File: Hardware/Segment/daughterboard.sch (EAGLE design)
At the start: 1 part, among them IC1 PBQ79656PAPTQ1

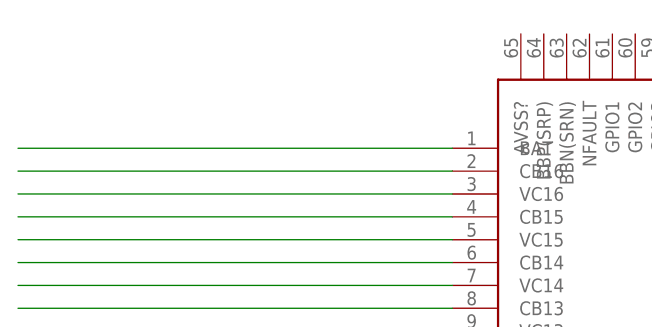
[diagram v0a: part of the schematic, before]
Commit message: added a resistor
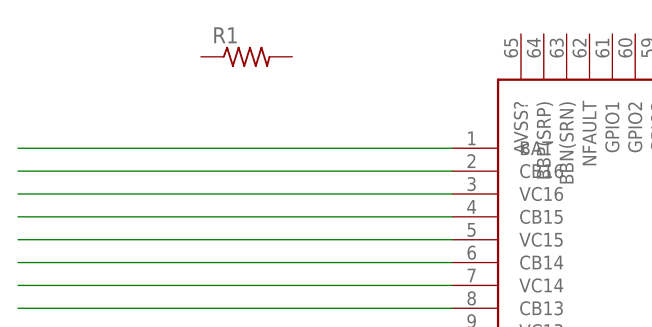
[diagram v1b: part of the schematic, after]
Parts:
- added R1: (no value), rcl:R-US_R0603
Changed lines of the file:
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@@
 <layers>
 <layer number="1" name="Top" color="4" fill="1" visible="no" active="no"/>
+<layer number="2" name="Route2" color="1" fill="3" visible="no" active="no"/>
+<layer number="3" name="Route3" color="4" fill="3" visible="no" active="no"/>
+<layer number="4" name="Route4" color="1" fill="4" visible="no" active="no"/>
+<layer number="5" name="Route5" color="4" fill="4" visible="no" active="no"/>
+<layer number="6" name="Route6" color="1" fill="8" visible="no" active="no"/>
+<layer number="7" name="Route7" color="4" fill="8" visible="no" active="no"/>
+<layer number="8" name="Route8" color="1" fill="2" visible="no" active="no"/>
+<layer number="9" name="Route9" color="4" fill="2" visible="no" active="no"/>
+<layer number="10" name="Route10" color="1" fill="7" visible="no" active="no"/>
+<layer number="11" name="Route11" color="4" fill="7" visible="no" active="no"/>
+<layer number="12" name="Route12" color="1" fill="5" visible="no" active="no"/>
+<layer number="13" name="Route13" color="4" fill="5" visible="no" active="no"/>
+<layer number="14" name="Route14" color="1" fill="6" visible="no" active="no"/>
+<layer number="15" name="Route15" color="4" fill="6" visible="no" active="no"/>
 <layer number="16" name="Bottom" color="1" fill="1" visible="no" active="no"/>
 <layer number="17" name="Pads" color="2" fill="1" visible="no" active="no"/>
@@
 <parts>
 <part name="IC1" library="PBQ79656PAPTQ1" deviceset="PBQ79656PAPTQ1" device=""/>
+<part name="R1" library="rcl" library_urn="urn:adsk.eagle:library:334" deviceset="R-US_" device="R0603" package3d_urn="urn:adsk.eagle:package:23555/3"/>
 </parts>
 <sheets>
@@
 <attribute name="VALUE" x="107.95" y="83.82" size="1.778" layer="96" align="center-left"/>
 </instance>
+<instance part="R1" gate="G$1" x="33.02" y="83.82" smashed="yes">
+<attribute name="NAME" x="29.21" y="85.3186" size="1.778" layer="95"/>
+<attribute name="VALUE" x="29.21" y="80.518" size="1.778" layer="96"/>
+</instance>
 </instances>
 <busses>
@@
 </schematic>
 </drawing>
+<compatibility>
+<note version="8.2" severity="warning">
+Since Version 8.2, EAGLE supports online libraries. The ids
+of those online libraries will not be understood (or retained)
+with this version.
+</note>
+<note version="8.3" severity="warning">
+Since Version 8.3, EAGLE supports URNs for individual library
+assets (packages, symbols, and devices). The URNs of those assets
+will not be understood (or retained) with this version.
+</note>
+<note version="8.3" severity="warning">
+Since Version 8.3, EAGLE supports the association of 3D packages
+with devices in libraries, schematics, and board files. Those 3D
+packages will not be understood (or retained) with this version.
+</note>
+<note version="8.4" severity="warning">
+Since Version 8.4, EAGLE supports properties for SPICE simulation.
+Probes in schematics and SPICE mapping objects found in parts and library devices
+will not be understood with this version. Update EAGLE to the latest version
+for full support of SPICE simulation.
+</note>
+</compatibility>
 </eagle>

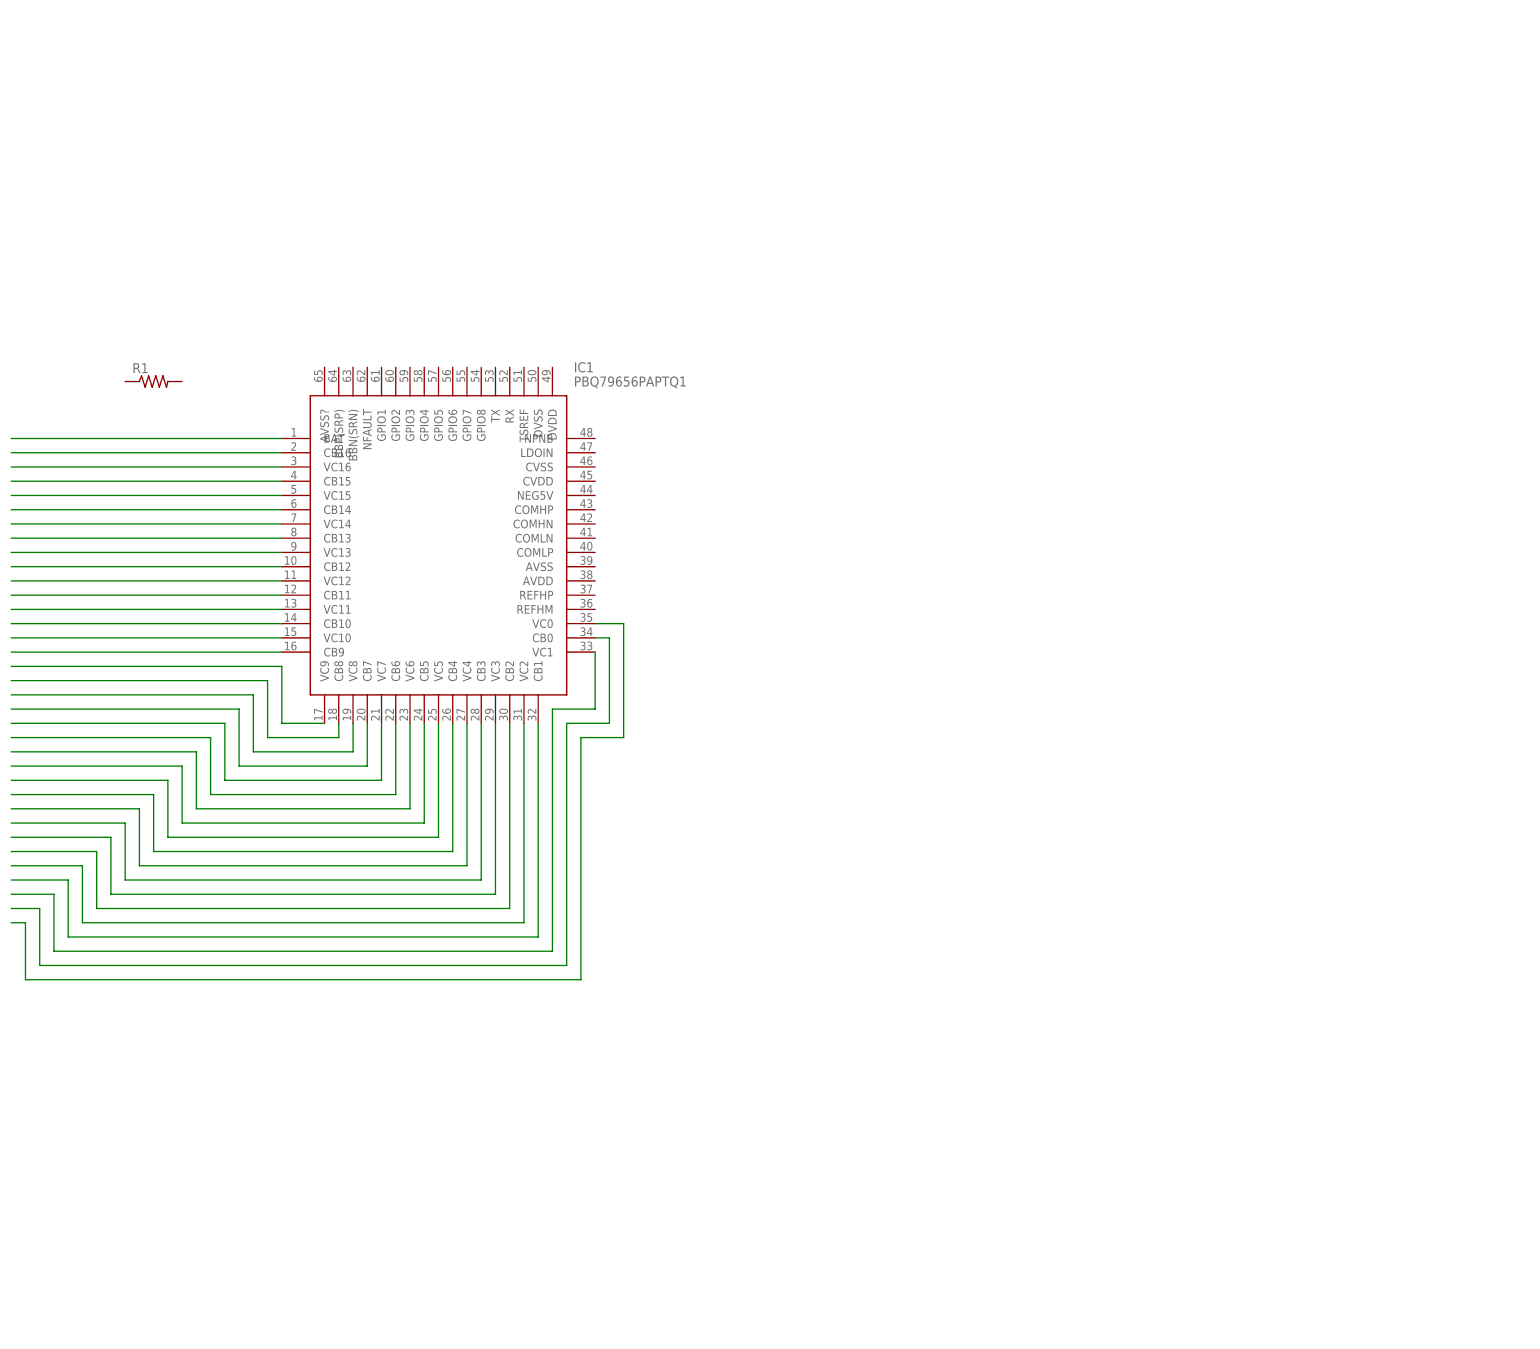
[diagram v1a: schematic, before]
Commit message: Connected IC to 10 battery cells
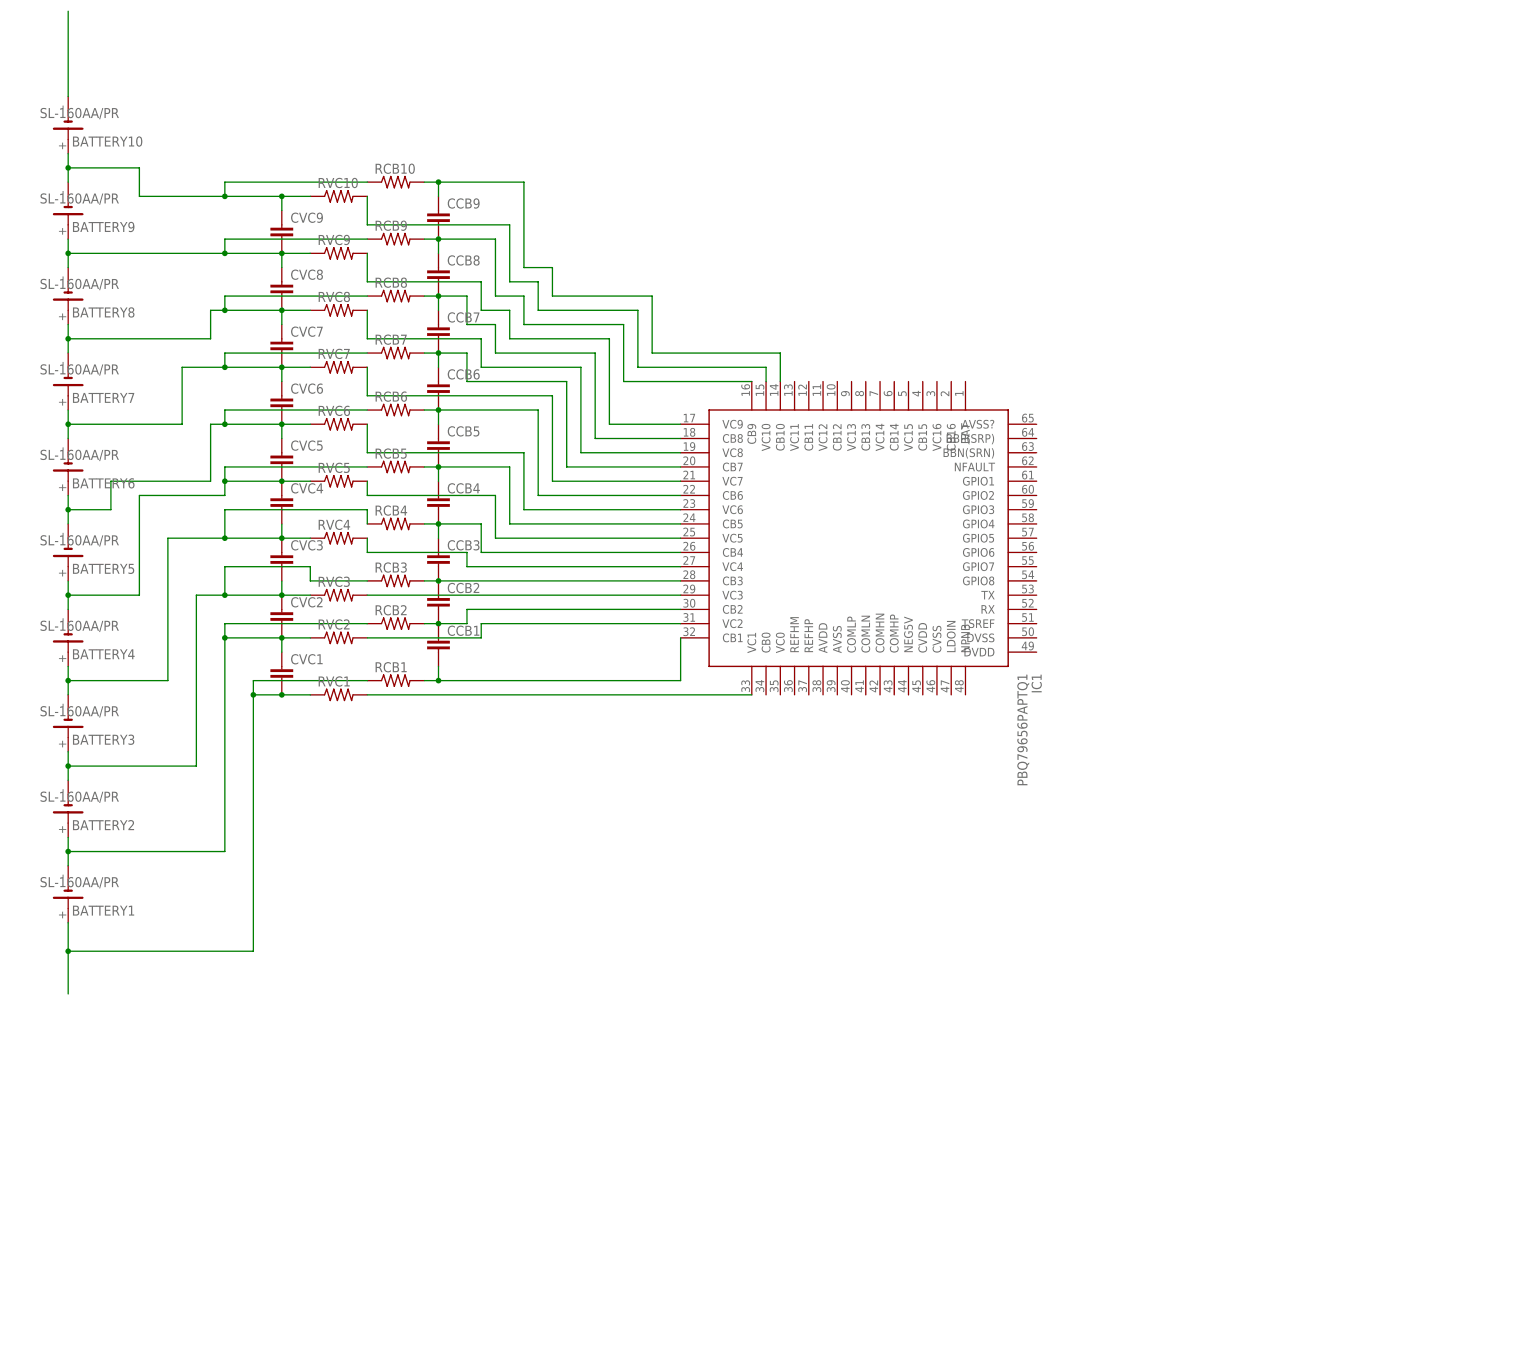
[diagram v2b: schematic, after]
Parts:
- removed R1: (no value), rcl:R-US_R0603
- added BATTERY1, BATTERY10, BATTERY2, BATTERY3, BATTERY4, BATTERY5, BATTERY6, BATTERY7, BATTERY8, BATTERY9: SL-160AA/PR, battery:SL-160AA/PR
- added CCB1, CCB2, CCB3, CCB4, CCB5, CCB6, CCB7, CCB8, CCB9, CVC1, CVC2, CVC3, CVC4, CVC5, CVC6, CVC7, CVC8, CVC9: (no value), capacitor-wima:C2.5/2
- added RCB1, RCB10, RCB2, RCB3, RCB4, RCB5, RCB6, RCB7, RCB8, RCB9, RVC1, RVC10, RVC2, RVC3, RVC4, RVC5, RVC6, RVC7, RVC8, RVC9: (no value), rcl:R-US_R0603
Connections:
- removed net N$25: IC1.VC5
- removed net N$33: IC1.VC1
- removed net N$34: IC1.CB0
- removed net N$35: IC1.VC0
- net N$1: now also IC1.VC1, RVC1.2; no longer IC1.BAT
- net N$10: now also IC1.VC4, RVC4.2; no longer IC1.CB12
- net N$11: now also CCB6.1, CCB7.2, IC1.CB7, RCB7.2; no longer IC1.VC12
- net N$12: now also BATTERY3.-, BATTERY4.+, CVC3.1, CVC4.2, RCB4.1, RVC4.1; no longer IC1.CB11
- net N$13: now also CCB3.1, CCB4.2, IC1.CB4, RCB4.2; no longer IC1.VC11
- net N$14: now also IC1.VC5, RVC5.2; no longer IC1.CB10
- net N$15: now also BATTERY4.-, BATTERY5.+, CVC4.1, CVC5.2, RCB5.1, RVC5.1; no longer IC1.VC10
- net N$16: now also CCB4.1, CCB5.2, IC1.CB5, RCB5.2; no longer IC1.CB9
- net N$17: now also IC1.VC8, RVC8.2; no longer IC1.VC9
- net N$18: now also BATTERY7.-, BATTERY8.+, CVC7.1, CVC8.2, RCB8.1, RVC8.1; no longer IC1.CB8
- net N$19: now also CCB7.1, CCB8.2, IC1.CB8, RCB8.2; no longer IC1.VC8
- net N$2: now also CCB1.2, IC1.CB1, RCB1.2; no longer IC1.CB16
- net N$20: now also IC1.VC9, RVC9.2; no longer IC1.CB7
- net N$21: now also BATTERY8.-, BATTERY9.+, CVC8.1, CVC9.2, RCB9.1, RVC9.1; no longer IC1.VC7
- net N$22: now also CCB8.1, CCB9.2, IC1.CB9, RCB9.2; no longer IC1.CB6
- net N$23: now also IC1.VC10, RVC10.2; no longer IC1.VC6
- net N$24: now also BATTERY10.-; no longer IC1.CB5
- net N$26: now also IC1.VC6, RVC6.2; no longer IC1.CB4
- net N$27: now also BATTERY5.-, BATTERY6.+, CVC5.1, CVC6.2, RCB6.1, RVC6.1; no longer IC1.VC4
- net N$28: now also CCB5.1, CCB6.2, IC1.CB6, RCB6.2; no longer IC1.CB3
- net N$29: now also BATTERY10.+, BATTERY9.-, CVC9.1, RCB10.1, RVC10.1; no longer IC1.VC3
- net N$3: now also IC1.VC2, RVC2.2; no longer IC1.VC16
- net N$30: now also IC1.VC7, RVC7.2; no longer IC1.CB2
- net N$31: now also BATTERY6.-, BATTERY7.+, CVC6.1, CVC7.2, RCB7.1, RVC7.1; no longer IC1.VC2
- net N$32: now also CCB9.1, IC1.CB10, RCB10.2; no longer IC1.CB1
- net N$4: now also CCB1.1, CCB2.2, IC1.CB2, RCB2.2; no longer IC1.CB15
- net N$5: now also BATTERY1.+, CVC1.2, RCB1.1, RVC1.1; no longer IC1.VC15
- net N$6: now also BATTERY1.-, BATTERY2.+, CVC1.1, CVC2.2, RCB2.1, RVC2.1; no longer IC1.CB14
- net N$7: now also CCB2.1, CCB3.2, IC1.CB3, RCB3.2; no longer IC1.VC14
- net N$8: now also BATTERY2.-, BATTERY3.+, CVC2.1, CVC3.2, RCB3.1, RVC3.1; no longer IC1.CB13
- net N$9: now also IC1.VC3, RVC3.2; no longer IC1.VC13
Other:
- moved on the sheet: IC1
